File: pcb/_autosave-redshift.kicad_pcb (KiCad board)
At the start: 4 copper layers, 45 x 63.5 mm, 75 parts, among them IC1 LPC5526JEV98, J1 USB_C_Receptacle_USB2.0, J2 Side, J3 Conn_01x06_Female, J4 Conn_ARM_JTAG_SWD_10, SW1 SW_SP, SW2 SW_SP, SW3 SW_SP, SW4 PTS810, U1 PAW3399DM‐T4QU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

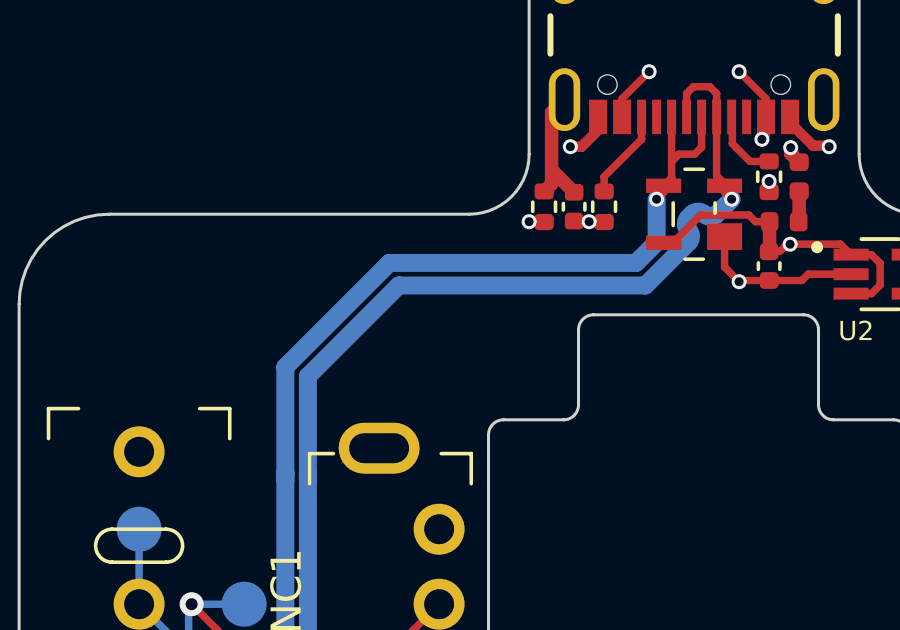
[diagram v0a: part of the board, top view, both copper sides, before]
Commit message: Small Changes to USB Footprint Make USB test points hopefully less detrimental
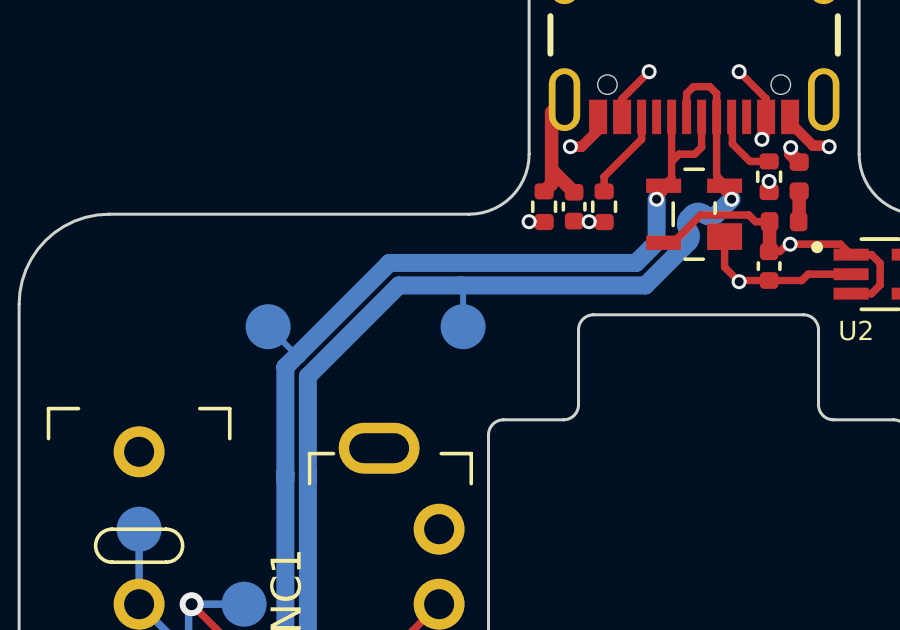
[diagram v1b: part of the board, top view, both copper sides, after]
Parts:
- added TP8: TestPoint, TestPoint:TestPoint_Pad_D1.5mm, B.Cu at (123.3, 68.8)
- added TP9: TestPoint, TestPoint:TestPoint_Pad_D1.5mm, B.Cu at (129.8, 68.8)
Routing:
- net /USB_D-: track 52.9 -> 54.3 mm
- net /USB_D+: track 52.7 -> 54.1 mm
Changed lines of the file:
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@@
+  )
+  (footprint "TestPoint:TestPoint_Pad_D1.5mm" (layer "B.Cu")
+    (at 129.8 68.75 180)
+    (descr "SMD pad as test Point, diameter 1.5mm")
+    (tags "test point SMD pad")
+    (property "Sheetfile" "redshift.kicad_sch")
+    (property "Sheetname" "")
+    (property "exclude_from_bom" "")
+    (attr exclude_from_pos_files exclude_from_bom)
+    (fp_text reference "TP9" (at 0 1.648) (layer "B.SilkS")
+      (effects (font (size 1 1) (thickness 0.15)) (justify mirror))
+    )
+    (fp_text value "TestPoint" (at 0 -1.75) (layer "B.Fab")
+      (effects (font (size 1 1) (thickness 0.15)) (justify mirror))
+    )
+    (fp_text user "${REFERENCE}" (at 0 1.65) (layer "B.Fab")
+      (effects (font (size 1 1) (thickness 0.15)) (justify mirror))
+    )
+    (fp_circle (center 0 0) (end 0 -0.95) (layer "B.SilkS") (width 0.12) (fill none))
+    (fp_circle (center 0 0) (end 1.25 0) (layer "B.CrtYd") (width 0.05) (fill none))
+    (pad "1" smd circle (at 0 0 180) (size 1.5 1.5) (layers "B.Cu" "B.Mask")
+      (net 7 "/USB_D-") (pinfunction "1") (pintype "passive"))
   )
   (footprint "TestPoint:TestPoint_Pad_D1.5mm" (layer "B.Cu")
@@
         (xy -0.652463 -0.52705)
       ) (layer "B.SilkS") (width 0) (fill solid))
+  )
+  (footprint "TestPoint:TestPoint_Pad_D1.5mm" (layer "B.Cu")
+    (at 123.3 68.75 180)
+    (descr "SMD pad as test Point, diameter 1.5mm")
+    (tags "test point SMD pad")
+    (property "Sheetfile" "redshift.kicad_sch")
+    (property "Sheetname" "")
+    (property "exclude_from_bom" "")
+    (attr exclude_from_pos_files exclude_from_bom)
+    (fp_text reference "TP8" (at 0 1.648) (layer "B.SilkS")
+      (effects (font (size 1 1) (thickness 0.15)) (justify mirror))
+    )
+    (fp_text value "TestPoint" (at 0 -1.75) (layer "B.Fab")
+      (effects (font (size 1 1) (thickness 0.15)) (justify mirror))
+    )
+    (fp_text user "${REFERENCE}" (at 0 1.65) (layer "B.Fab")
+      (effects (font (size 1 1) (thickness 0.15)) (justify mirror))
+    )
+    (fp_circle (center 0 0) (end 0 -0.95) (layer "B.SilkS") (width 0.12) (fill none))
+    (fp_circle (center 0 0) (end 1.25 0) (layer "B.CrtYd") (width 0.05) (fill none))
+    (pad "1" smd circle (at 0 0 180) (size 1.5 1.5) (layers "B.Cu" "B.Mask")
+      (net 6 "/USB_D+") (pinfunction "1") (pintype "passive"))
   )
   (footprint "TestPoint:TestPoint_Pad_D1.5mm" (layer "B.Cu")
@@
   (via (at 136.25 64.5) (size 0.5) (drill 0.3) (layers "F.Cu" "B.Cu") (free) (net 6))
   (via (at 138.05 91) (size 0.5) (drill 0.3) (layers "F.Cu" "B.Cu") (free) (net 6))
+  (segment (start 124.284834 69.684834) (end 123.875 70.094668) (width 0.6) (layer "B.Cu") (net 6))
   (segment (start 123.875 73.875) (end 123.875 73.625) (width 0.6) (layer "B.Cu") (net 6))
   (segment (start 136.695886 89.1) (end 136.5 89.1) (width 0.25) (layer "B.Cu") (net 6))
   (segment (start 135.564339 66.625) (end 127.344668 66.625) (width 0.6) (layer "B.Cu") (net 6))
+  (segment (start 123.3 68.75) (end 124.234834 69.684834) (width 0.2) (layer "B.Cu") (net 6))
   (segment (start 138.05 91) (end 138.05 90.454114) (width 0.25) (layer "B.Cu") (net 6))
+  (segment (start 124.234834 69.684834) (end 124.284834 69.684834) (width 0.2) (layer "B.Cu") (net 6))
   (segment (start 136.25 65.939339) (end 135.564339 66.625) (width 0.6) (layer "B.Cu") (net 6))
   (segment (start 136.25 64.5) (end 136.25 65.939339) (width 0.6) (layer "B.Cu") (net 6))
-  (segment (start 127.344668 66.625) (end 123.875 70.094668) (width 0.6) (layer "B.Cu") (net 6))
+  (segment (start 127.344668 66.625) (end 124.284834 69.684834) (width 0.6) (layer "B.Cu") (net 6))
   (segment (start 123.875 70.094668) (end 123.875 73.625) (width 0.6) (layer "B.Cu") (net 6))
   (segment (start 123.875 73.625) (end 123.875 83.905332) (width 0.6) (layer "B.Cu") (net 6))
@@
   (via (at 138.75 64.5) (size 0.5) (drill 0.3) (layers "F.Cu" "B.Cu") (free) (net 7))
   (segment (start 138 89) (end 137.35 89) (width 0.25) (layer "B.Cu") (net 7))
+  (segment (start 135.875 67.375) (end 129.725 67.375) (width 0.6) (layer "B.Cu") (net 7))
   (segment (start 137.428437 64.999999) (end 137.308887 65.119548) (width 0.6) (layer "B.Cu") (net 7))
   (segment (start 137.101498 66.148502) (end 135.875 67.375) (width 0.6) (layer "B.Cu") (net 7))
+  (segment (start 129.8 67.45) (end 129.725 67.375) (width 0.2) (layer "B.Cu") (net 7))
   (segment (start 127.655332 67.375) (end 124.625 70.405332) (width 0.6) (layer "B.Cu") (net 7))
-  (segment (start 135.875 67.375) (end 127.655332 67.375) (width 0.6) (layer "B.Cu") (net 7))
   (segment (start 137.839219 65) (end 137.839218 64.999999) (width 0.6) (layer "B.Cu") (net 7))
   (segment (start 124.625 70.405332) (end 124.625 73.625) (width 0.6) (layer "B.Cu") (net 7))
   (segment (start 137.428437 64.999998) (end 137.428437 64.999999) (width 0.6) (layer "B.Cu") (net 7))
+  (segment (start 129.725 67.375) (end 127.655332 67.375) (width 0.6) (layer "B.Cu") (net 7))
   (segment (start 137.308888 65.94111) (end 137.308887 65.94111) (width 0.6) (layer "B.Cu") (net 7))
   (segment (start 137.308888 65.530329) (end 137.308887 65.530329) (width 0.6) (layer "B.Cu") (net 7))
   (segment (start 129.380332 88.35) (end 136.7 88.35) (width 0.6) (layer "B.Cu") (net 7))
   (segment (start 137.839218 65) (end 137.839219 65) (width 0.6) (layer "B.Cu") (net 7))
+  (segment (start 129.8 68.75) (end 129.8 67.45) (width 0.2) (layer "B.Cu") (net 7))
   (segment (start 128.951546 87.921214) (end 129.380332 88.35) (width 0.6) (layer "B.Cu") (net 7))
   (segment (start 124.625 83.594668) (end 128.951546 87.921214) (width 0.6) (layer "B.Cu") (net 7))
